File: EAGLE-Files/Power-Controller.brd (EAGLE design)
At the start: 34.3 x 47.9 mm, 12 parts

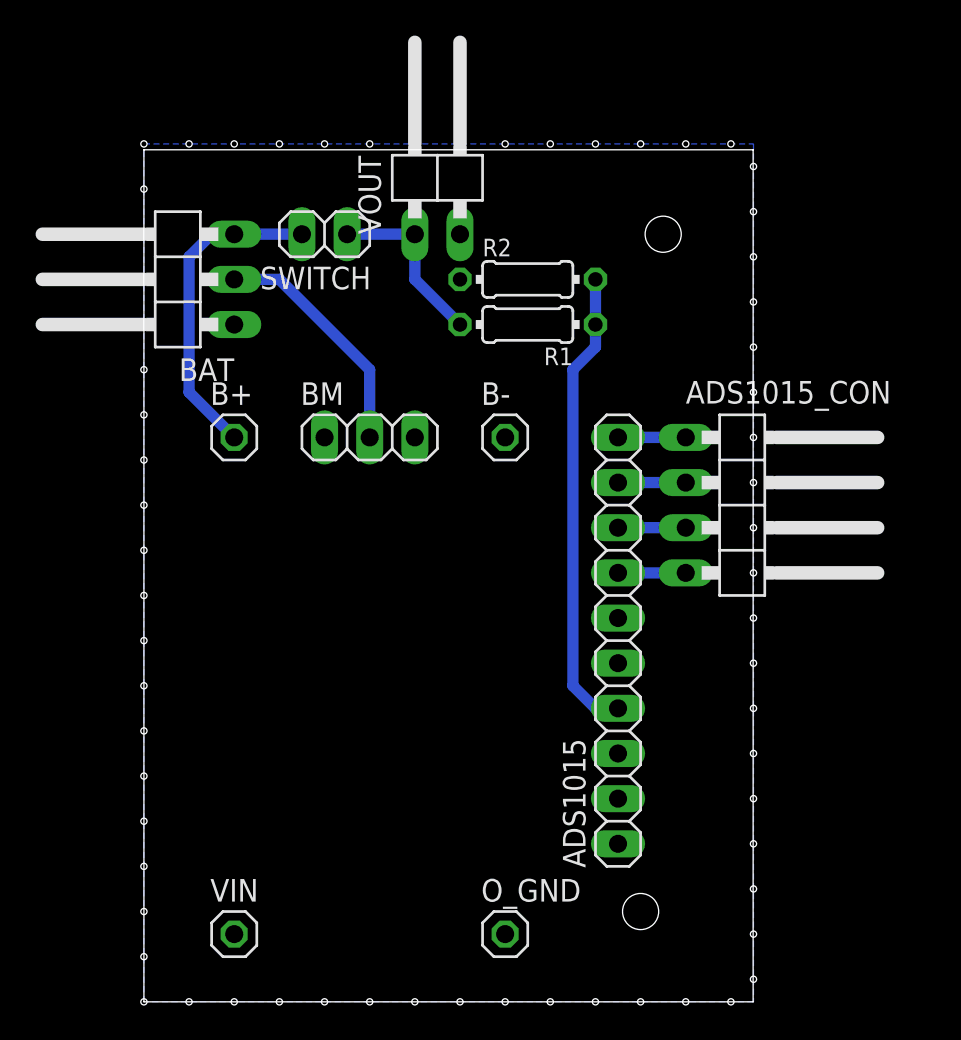
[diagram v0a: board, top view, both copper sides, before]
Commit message: Updated all boards for JLCPCB order
Also added the controller boards and schematics back
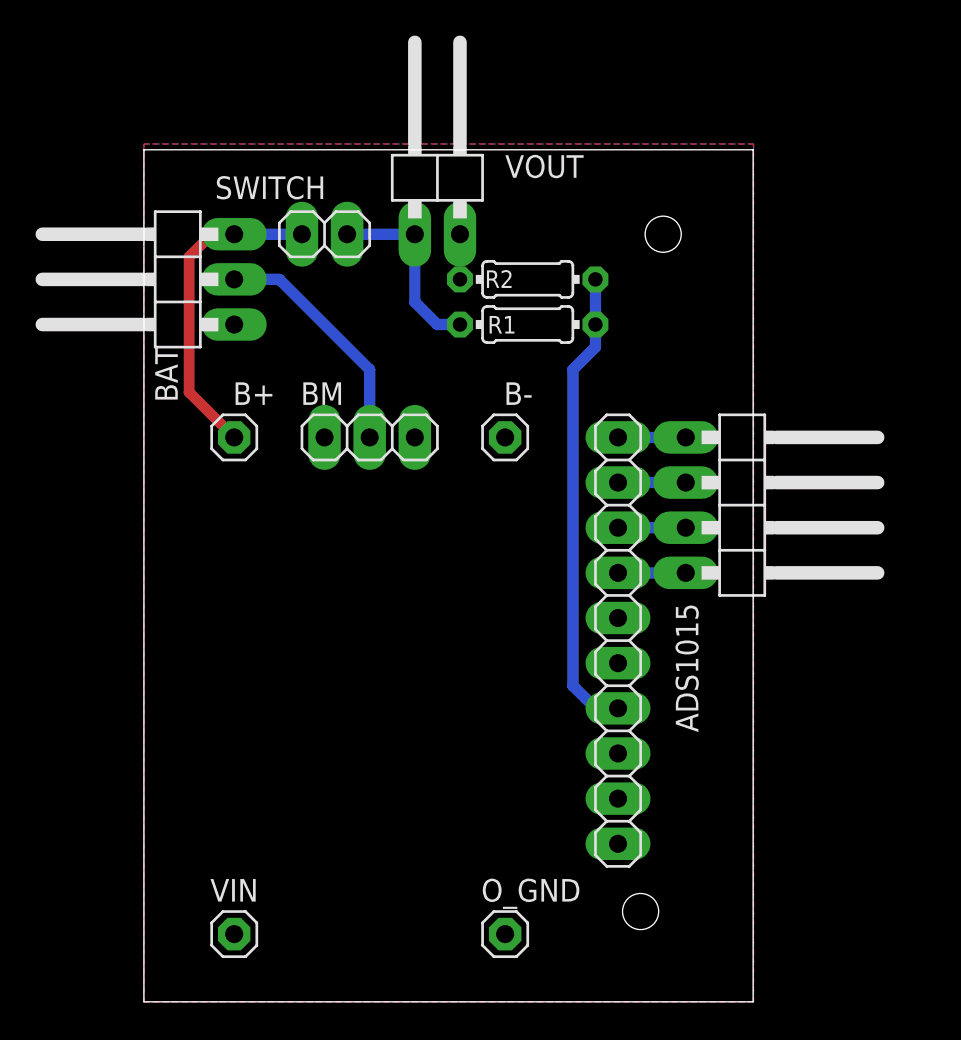
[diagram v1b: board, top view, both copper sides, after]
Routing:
- net N$4: track 9.94 -> 10.7 mm
- added copper zone on layer 1, net GND
